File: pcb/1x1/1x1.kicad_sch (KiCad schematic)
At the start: 9 parts, among them J1 Conn_02x04_Odd_Even

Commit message: 1x1 pcb updated
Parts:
- removed H1, H2, H3, H4, H5, H6, H7, H8: MountingHole_Pad, Connector_Wire:SolderWirePad_1x01_SMD_1x2mm, symbol Mechanical:MountingHole_Pad
- added RV1: R_Potentiometer, symbol Device:R_Potentiometer
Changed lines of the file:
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@@
-    (stroke (width 0) (type default))
-  )
-  (wire (pts (xy 123.825 88.265) (xy 128.905 88.265))
-    (stroke (width 0) (type default))
-  )
-  (wire (pts (xy 116.205 81.915) (xy 116.205 94.615))
     (stroke (width 0) (type default))
   )
   (wire (pts (xy 121.285 69.215) (xy 121.285 61.595))
-    (stroke (width 0) (type default))
-  )
-  (wire (pts (xy 128.905 88.265) (xy 128.905 94.615))
-    (stroke (width 0) (type default))
-  )
-  (wire (pts (xy 118.745 94.615) (xy 118.745 81.915))
     (stroke (width 0) (type default))
   )
@@
     (stroke (width 0) (type default))
   )
-  (wire (pts (xy 121.285 94.615) (xy 123.825 94.615))
-    (stroke (width 0) (type default))
-  )
   (wire (pts (xy 121.285 61.595) (xy 122.555 61.595))
     (stroke (width 0) (type default))
@@
     (stroke (width 0) (type default))
   )
-  (wire (pts (xy 116.205 94.615) (xy 113.665 94.615))
-    (stroke (width 0) (type default))
-  )
   (wire (pts (xy 123.825 61.595) (xy 127.635 61.595))
-    (stroke (width 0) (type default))
-  )
-  (wire (pts (xy 123.825 81.915) (xy 123.825 88.265))
     (stroke (width 0) (type default))
   )
   (wire (pts (xy 118.745 69.215) (xy 118.745 61.595))
     (stroke (width 0) (type default))
-  )
-  (wire (pts (xy 121.285 81.915) (xy 121.285 94.615))
-    (stroke (width 0) (type default))
-  )
-  (symbol (lib_id "Mechanical:MountingHole_Pad") (at 127.635 59.055 0) (unit 1)
-    (in_bom yes) (on_board yes) (dnp no) (fields_autoplaced)
-    (property "Reference" "H8" (at 126.365 55.245 90)
-      (effects (font (size 1.27 1.27)) (justify left))
-    )
-    (property "Value" "MountingHole_Pad" (at 128.905 55.245 90)
-      (effects (font (size 1.27 1.27)) (justify left))
-    )
-    (property "Footprint" "Connector_Wire:SolderWirePad_1x01_SMD_1x2mm" (at 127.635 59.055 0)
-      (effects (font (size 1.27 1.27)) hide)
-    )
-    (property "Datasheet" "~" (at 127.635 59.055 0)
-      (effects (font (size 1.27 1.27)) hide)
-    )
-    (pin "1")
-    (instances
-      (project "1x1"
-        (path "/4badd998-baa9-4f60-ad99-cdcaa0ecdce6"
-          (reference "H8") (unit 1)
-        )
-      )
-    )
-  )
-  (symbol (lib_id "Mechanical:MountingHole_Pad") (at 128.905 97.155 180) (unit 1)
-    (in_bom yes) (on_board yes) (dnp no) (fields_autoplaced)
-    (property "Reference" "H4" (at 122.555 98.425 90)
-      (effects (font (size 1.27 1.27)))
-    )
-    (property "Value" "MountingHole_Pad" (at 125.095 98.425 90)
-      (effects (font (size 1.27 1.27)))
-    )
-    (property "Footprint" "Connector_Wire:SolderWirePad_1x01_SMD_1x2mm" (at 128.905 97.155 0)
-      (effects (font (size 1.27 1.27)) hide)
-    )
-    (property "Datasheet" "~" (at 128.905 97.155 0)
-      (effects (font (size 1.27 1.27)) hide)
-    )
-    (pin "1")
-    (instances
-      (project "1x1"
-        (path "/4badd998-baa9-4f60-ad99-cdcaa0ecdce6"
-          (reference "H4") (unit 1)
-        )
-      )
-    )
-  )
-  (symbol (lib_id "Mechanical:MountingHole_Pad") (at 122.555 59.055 0) (unit 1)
-    (in_bom yes) (on_board yes) (dnp no) (fields_autoplaced)
-    (property "Reference" "H7" (at 121.285 55.245 90)
-      (effects (font (size 1.27 1.27)) (justify left))
-    )
-    (property "Value" "MountingHole_Pad" (at 123.825 55.245 90)
-      (effects (font (size 1.27 1.27)) (justify left))
-    )
-    (property "Footprint" "Connector_Wire:SolderWirePad_1x01_SMD_1x2mm" (at 122.555 59.055 0)
-      (effects (font (size 1.27 1.27)) hide)
-    )
-    (property "Datasheet" "~" (at 122.555 59.055 0)
-      (effects (font (size 1.27 1.27)) hide)
-    )
-    (pin "1")
-    (instances
-      (project "1x1"
-        (path "/4badd998-baa9-4f60-ad99-cdcaa0ecdce6"
-          (reference "H7") (unit 1)
-        )
-      )
-    )
-  )
-  (symbol (lib_id "Mechanical:MountingHole_Pad") (at 113.665 59.055 0) (unit 1)
-    (in_bom yes) (on_board yes) (dnp no) (fields_autoplaced)
-    (property "Reference" "H5" (at 112.395 55.245 90)
-      (effects (font (size 1.27 1.27)) (justify left))
-    )
-    (property "Value" "MountingHole_Pad" (at 114.935 55.245 90)
-      (effects (font (size 1.27 1.27)) (justify left))
-    )
-    (property "Footprint" "Connector_Wire:SolderWirePad_1x01_SMD_1x2mm" (at 113.665 59.055 0)
-      (effects (font (size 1.27 1.27)) hide)
-    )
-    (property "Datasheet" "~" (at 113.665 59.055 0)
-      (effects (font (size 1.27 1.27)) hide)
-    )
-    (pin "1")
-    (instances
-      (project "1x1"
-        (path "/4badd998-baa9-4f60-ad99-cdcaa0ecdce6"
-          (reference "H5") (unit 1)
-        )
-      )
-    )
   )
   (symbol (lib_id "Connector_Generic:Conn_02x04_Odd_Even") (at 118.745 76.835 90) (unit 1)
@@
     )
   )
-  (symbol (lib_id "Mechanical:MountingHole_Pad") (at 113.665 97.155 180) (unit 1)
+  (symbol (lib_id "Device:R_Potentiometer") (at 119.38 86.36 90) (unit 1)
     (in_bom yes) (on_board yes) (dnp no) (fields_autoplaced)
-    (property "Reference" "H1" (at 107.315 98.425 90)
+    (property "Reference" "RV1" (at 119.38 90.17 90)
       (effects (font (size 1.27 1.27)))
     )
-    (property "Value" "MountingHole_Pad" (at 109.855 98.425 90)
+    (property "Value" "R_Potentiometer" (at 119.38 92.71 90)
       (effects (font (size 1.27 1.27)))
     )
-    (property "Footprint" "Connector_Wire:SolderWirePad_1x01_SMD_1x2mm" (at 113.665 97.155 0)
+    (property "Footprint" "" (at 119.38 86.36 0)
       (effects (font (size 1.27 1.27)) hide)
     )
-    (property "Datasheet" "~" (at 113.665 97.155 0)
+    (property "Datasheet" "~" (at 119.38 86.36 0)
       (effects (font (size 1.27 1.27)) hide)
     )
     (pin "1")
+    (pin "3")
+    (pin "2")
     (instances
       (project "1x1"
         (path "/4badd998-baa9-4f60-ad99-cdcaa0ecdce6"
-          (reference "H1") (unit 1)
+          (reference "RV1") (unit 1)
         )
       )
-    )
-  )
-  (symbol (lib_id "Mechanical:MountingHole_Pad") (at 117.475 59.055 0) (unit 1)
-    (in_bom yes) (on_board yes) (dnp no) (fields_autoplaced)
-    (property "Reference" "H6" (at 116.205 55.245 90)
-      (effects (font (size 1.27 1.27)) (justify left))
-    )
-    (property "Value" "MountingHole_Pad" (at 118.745 55.245 90)
-      (effects (font (size 1.27 1.27)) (justify left))
-    )
-    (property "Footprint" "Connector_Wire:SolderWirePad_1x01_SMD_1x2mm" (at 117.475 59.055 0)
-      (effects (font (size 1.27 1.27)) hide)
-    )
-    (property "Datasheet" "~" (at 117.475 59.055 0)
-      (effects (font (size 1.27 1.27)) hide)
-    )
-    (pin "1")
-    (instances
-      (project "1x1"
-        (path "/4badd998-baa9-4f60-ad99-cdcaa0ecdce6"
-          (reference "H6") (unit 1)
-        )
-      )
-    )
-  )
-  (symbol (lib_id "Mechanical:MountingHole_Pad") (at 123.825 97.155 180) (unit 1)
-    (in_bom yes) (on_board yes) (dnp no) (fields_autoplaced)
-    (property "Reference" "H3" (at 117.475 98.425 90)
-      (effects (font (size 1.27 1.27)))
-    )
-    (property "Value" "MountingHole_Pad" (at 120.015 98.425 90)
-      (effects (font (size 1.27 1.27)))
-    )
-    (property "Footprint" "Connector_Wire:SolderWirePad_1x01_SMD_1x2mm" (at 123.825 97.155 0)
-      (effects (font (size 1.27 1.27)) hide)
-    )
-    (property "Datasheet" "~" (at 123.825 97.155 0)
-      (effects (font (size 1.27 1.27)) hide)
-    )
-    (pin "1")
-    (instances
-      (project "1x1"
-        (path "/4badd998-baa9-4f60-ad99-cdcaa0ecdce6"
-          (reference "H3") (unit 1)
-        )
-      )
-    )
-  )
-  (symbol (lib_id "Mechanical:MountingHole_Pad") (at 118.745 97.155 180) (unit 1)
-    (in_bom yes) (on_board yes) (dnp no) (fields_autoplaced)
-    (property "Reference" "H2" (at 112.395 98.425 90)
-      (effects (font (size 1.27 1.27)))
-    )
-    (property "Value" "MountingHole_Pad" (at 114.935 98.425 90)
-      (effects (font (size 1.27 1.27)))
-    )
-    (property "Footprint" "Connector_Wire:SolderWirePad_1x01_SMD_1x2mm" (at 118.745 97.155 0)
-      (effects (font (size 1.27 1.27)) hide)
-    )
-    (property "Datasheet" "~" (at 118.745 97.155 0)
-      (effects (font (size 1.27 1.27)) hide)
-    )
-    (pin "1")
-    (instances
-      (project "1x1"
-        (path "/4badd998-baa9-4f60-ad99-cdcaa0ecdce6"
-          (reference "H2") (unit 1)
-        )
-      )

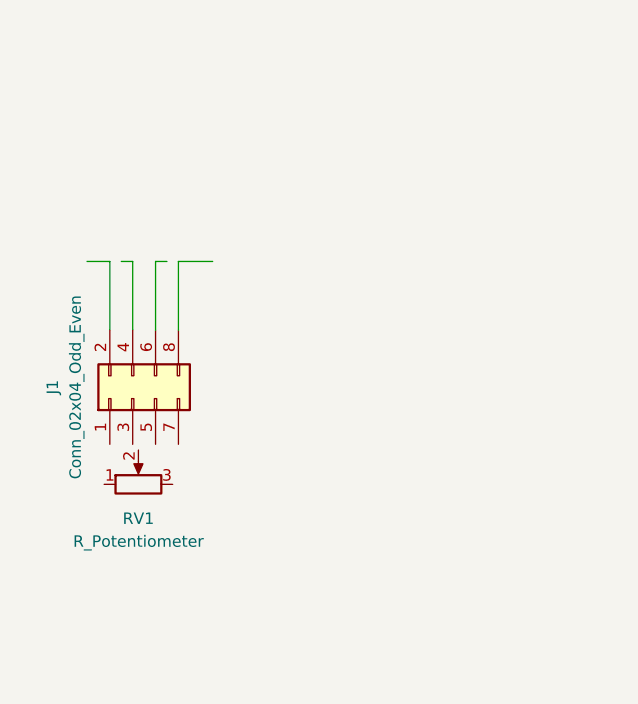
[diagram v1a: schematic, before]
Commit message: kicad version 8.0, 1x1 pcb
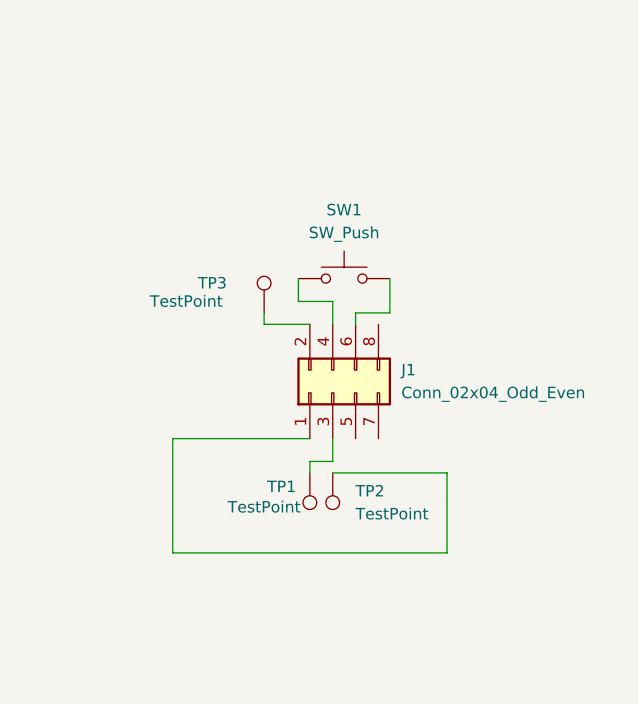
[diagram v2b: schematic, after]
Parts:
- removed RV1: R_Potentiometer, symbol Device:R_Potentiometer
- added SW1: SW_Push, PCM_Switch_Keyboard_Cherry_MX:SW_Cherry_MX_Plate, symbol Switch:SW_Push
- added TP1, TP2, TP3: TestPoint, TestPoint:TestPoint_Pad_1.5x1.5mm, symbol Connector:TestPoint
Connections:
- net at J1.1 (Pin_1): now also TP2.1
- net at J1.2 (Pin_2): now also TP3.1
- net at J1.3 (Pin_3): now also TP1.1
- net at J1.4 (Pin_4): now also SW1.1
- net at J1.6 (Pin_6): now also SW1.2
